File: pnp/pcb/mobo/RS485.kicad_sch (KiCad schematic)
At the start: 4 parts, among them J17 Feeders, U14 MAX3078E

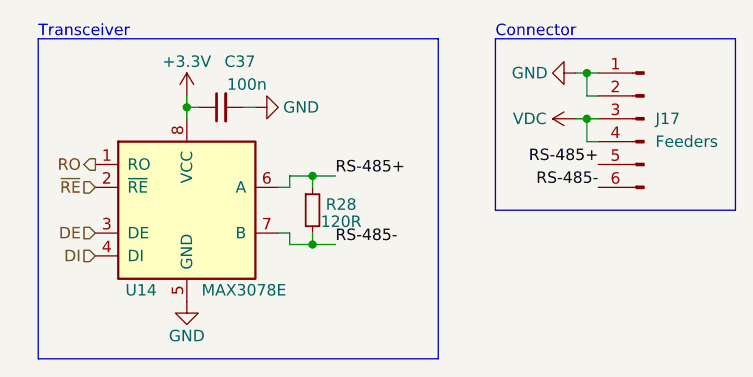
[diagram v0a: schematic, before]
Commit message: tweak PN of mobo
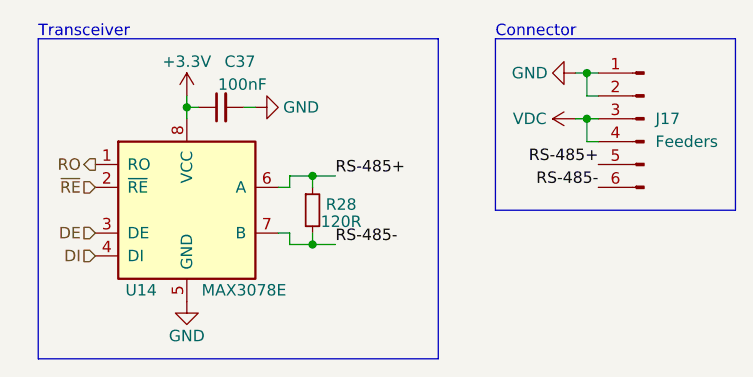
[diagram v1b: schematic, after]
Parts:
- C37: value 100n -> 100nF
- R28: LCSC C131390 -> C139879
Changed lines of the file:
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@@
       (effects (font (size 1.27 1.27)) hide)
     )
-    (property "LCSC" "C131390 " (at 144.78 106.68 0)
+    (property "LCSC" "C139879" (at 144.78 106.68 0)
       (effects (font (size 1.27 1.27)) hide)
     )
@@
       (effects (font (size 1.27 1.27)) (justify left))
     )
-    (property "Value" "100n" (at 139.7 92.71 90)
+    (property "Value" "100nF" (at 139.7 92.71 90)
       (effects (font (size 1.27 1.27)) (justify left))
     )
